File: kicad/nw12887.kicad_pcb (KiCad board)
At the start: 2 copper layers, 18.3 x 30.9 mm, 4 parts, among them U1 ds12887, U2 ds12887, Y1 Crystal_Small

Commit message: Silk layer changes, added lables
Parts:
- BT1: value Battery_Cell -> CR2025
- U1: value ds12887 -> bq3285
- Y1: value Crystal_Small -> 32kHz 6pF
- moved BT1 1.27 mm to (134.6, 97.2)

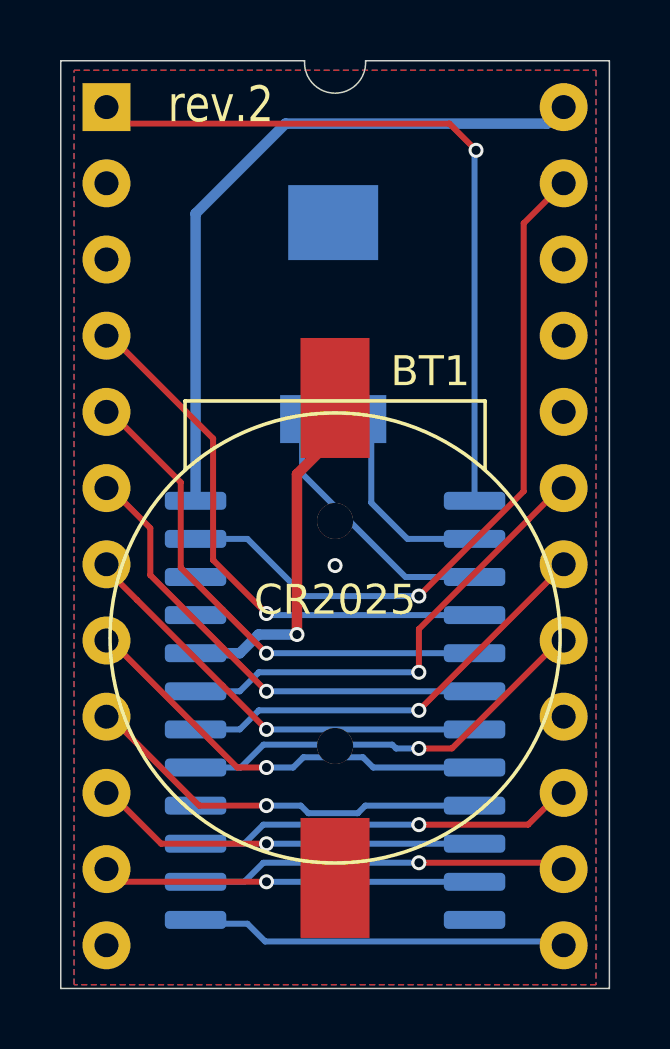
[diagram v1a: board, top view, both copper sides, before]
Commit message: Fixed battery socket position
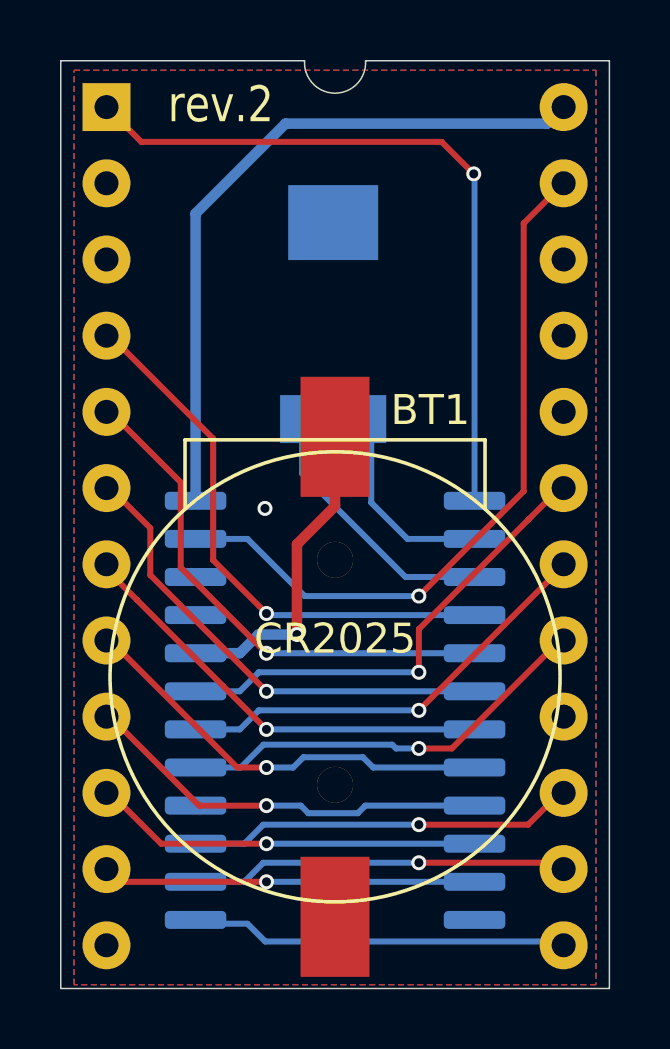
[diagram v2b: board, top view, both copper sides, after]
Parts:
- moved BT1 1.30 mm to (134.6, 98.5)
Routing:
- net MOT: track 24.6 -> 24.1 mm
- net GND: vias 1 -> 0
- net (no net): vias 0 -> 1
